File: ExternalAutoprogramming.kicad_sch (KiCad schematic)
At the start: 1 part, among them J4 Conn_01x04_Socket

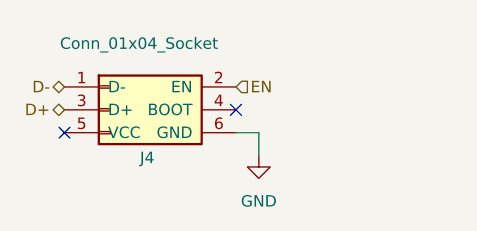
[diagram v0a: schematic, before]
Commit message: feat: Disconnect EN pin from external autoprogramming
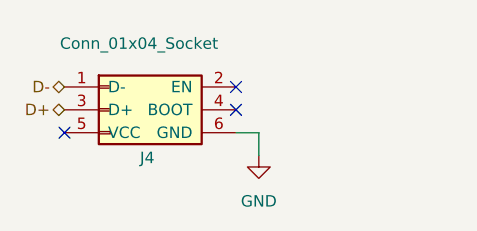
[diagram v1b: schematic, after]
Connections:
- net EN: no longer names the net of J4.2 (EN)
- no-connect marks 2 -> 3
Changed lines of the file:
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@@
 		(at 149.86 99.06)
+	)
+	(no_connect
+		(at 168.91 93.98)
 	)
 	(wire
@@
 		)
 	)
-	(hierarchical_label "EN"
-		(shape input)
-		(at 168.91 93.98 0)
-		(effects
-			(font
-				(size 1.27 1.27)
-			)
-			(justify left)
-		)
-	)

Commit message: feat: Replace autoprogramming symbol with Conn_02x03
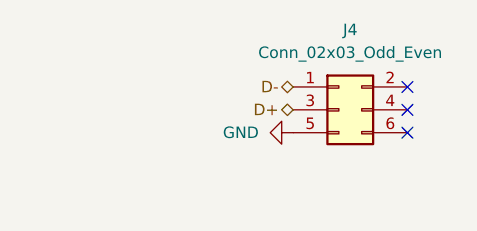
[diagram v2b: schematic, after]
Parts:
- J4: value Conn_01x04_Socket -> Conn_02x03_Odd_Even
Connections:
- net GND: now also J4.5 (Pin_5); no longer J4.6 (GND)
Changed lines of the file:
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@@
 	)
 	(no_connect
-		(at 168.91 96.52)
+		(at 187.96 99.06)
 	)
 	(no_connect
-		(at 149.86 99.06)
+		(at 187.96 93.98)
 	)
 	(no_connect
-		(at 168.91 93.98)
-	)
-	(wire
-		(pts
-			(xy 171.45 99.06) (xy 168.91 99.06)
-		)
-		(stroke
-			(width 0)
-			(type default)
-		)
-	)
-	(wire
-		(pts
-			(xy 171.45 101.6) (xy 171.45 99.06)
-		)
-		(stroke
-			(width 0)
-			(type default)
-		)
+		(at 187.96 96.52)
 	)
 	(hierarchical_label "D+"
 		(shape bidirectional)
-		(at 149.86 96.52 180)
+		(at 175.26 96.52 180)
 		(effects
 			(font
@@
 	(hierarchical_label "D-"
 		(shape bidirectional)
-		(at 149.86 93.98 180)
+		(at 175.26 93.98 180)
 		(effects
 			(font
@@
 	)
 	(symbol
+		(lib_name "Conn_02x03_Odd_Even_1")
 		(lib_id "Connector_Generic:Conn_02x03_Odd_Even")
-		(at 154.94 96.52 0)
+		(at 180.34 96.52 0)
 		(unit 1)
 		(body_style 1)
@@
 		(in_pos_files yes)
 		(dnp no)
+		(fields_autoplaced yes)
 		(property "Reference" "J4"
-			(at 158.242 101.854 0)
+			(at 181.61 87.63 0)
 			(show_name no)
 			(do_not_autoplace no)
@@
 					(size 1.27 1.27)
 				)
-				(justify left)
 			)
 		)
-		(property "Value" "Conn_01x04_Socket"
-			(at 149.352 89.154 0)
+		(property "Value" "Conn_02x03_Odd_Even"
+			(at 181.61 90.17 0)
 			(show_name no)
 			(do_not_autoplace no)
@@
 					(size 1.27 1.27)
 				)
-				(justify left)
 			)
 		)
 		(property "Footprint" "Connector:Tag-Connect_TC2030-IDC-NL_2x03_P1.27mm_Vertical"
-			(at 154.94 83.058 0)
+			(at 180.34 96.52 0)
 			(hide yes)
 			(show_name no)
@@
 		)
 		(property "Datasheet" ""
-			(at 154.94 96.52 0)
+			(at 180.34 96.52 0)
 			(hide yes)
 			(show_name no)
@@
 		)
 		(property "Description" "Generic connector, double row, 02x03, odd/even pin numbering scheme (row 1 odd numbers, row 2 even numbers), script generated (kicad-library-utils/schlib/autogen/connector/)"
-			(at 156.21 86.36 0)
+			(at 180.34 96.52 0)
 			(hide yes)
 			(show_name no)
@@
 			)
 		)
-		(pin "1"
-		)
-		(pin "2"
-		)
-		(pin "3"
-		)
 		(pin "4"
 		)
 		(pin "5"
 		)
+		(pin "2"
+		)
 		(pin "6"
+		)
+		(pin "1"
+		)
+		(pin "3"
 		)
 		(instances
@@
 	(symbol
 		(lib_id "power:GND")
-		(at 171.45 101.6 0)
-		(mirror y)
+		(at 175.26 99.06 270)
+		(mirror x)
 		(unit 1)
 		(body_style 1)
@@
 		(dnp no)
 		(fields_autoplaced yes)
-		(property "Reference" "#PWR05"
-			(at 171.45 107.95 0)
+		(property "Reference" "#PWR015"
+			(at 168.91 99.06 0)
 			(hide yes)
 			(show_name no)
@@
 		)
 		(property "Value" "GND"
-			(at 171.45 106.68 0)
+			(at 171.45 99.0599 90)
 			(show_name no)
 			(do_not_autoplace no)
@@
 					(size 1.27 1.27)
 				)
+				(justify right)
 			)
 		)
 		(property "Footprint" ""
-			(at 171.45 101.6 0)
+			(at 175.26 99.06 0)
 			(hide yes)
 			(show_name no)
@@
 		)
 		(property "Datasheet" ""
-			(at 171.45 101.6 0)
+			(at 175.26 99.06 0)
 			(hide yes)
 			(show_name no)
@@
 		)
 		(property "Description" "Power symbol creates a global label with name \"GND\" , ground"
-			(at 171.45 101.6 0)
+			(at 175.26 99.06 0)
 			(hide yes)
 			(show_name no)
@@
 			(project "Vent"
 				(path "/44080430-3c3a-4a58-87da-65c26034d41d/baa2a2d6-ded2-444d-b992-886e8249722c"
-					(reference "#PWR05")
+					(reference "#PWR015")
 					(unit 1)
 				)
